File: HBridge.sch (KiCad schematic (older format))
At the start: 35 parts, among them Q1 RTQ020N03, Q2 RTQ020N03, Q3 RTQ020N03, Q4 RTQ020N03

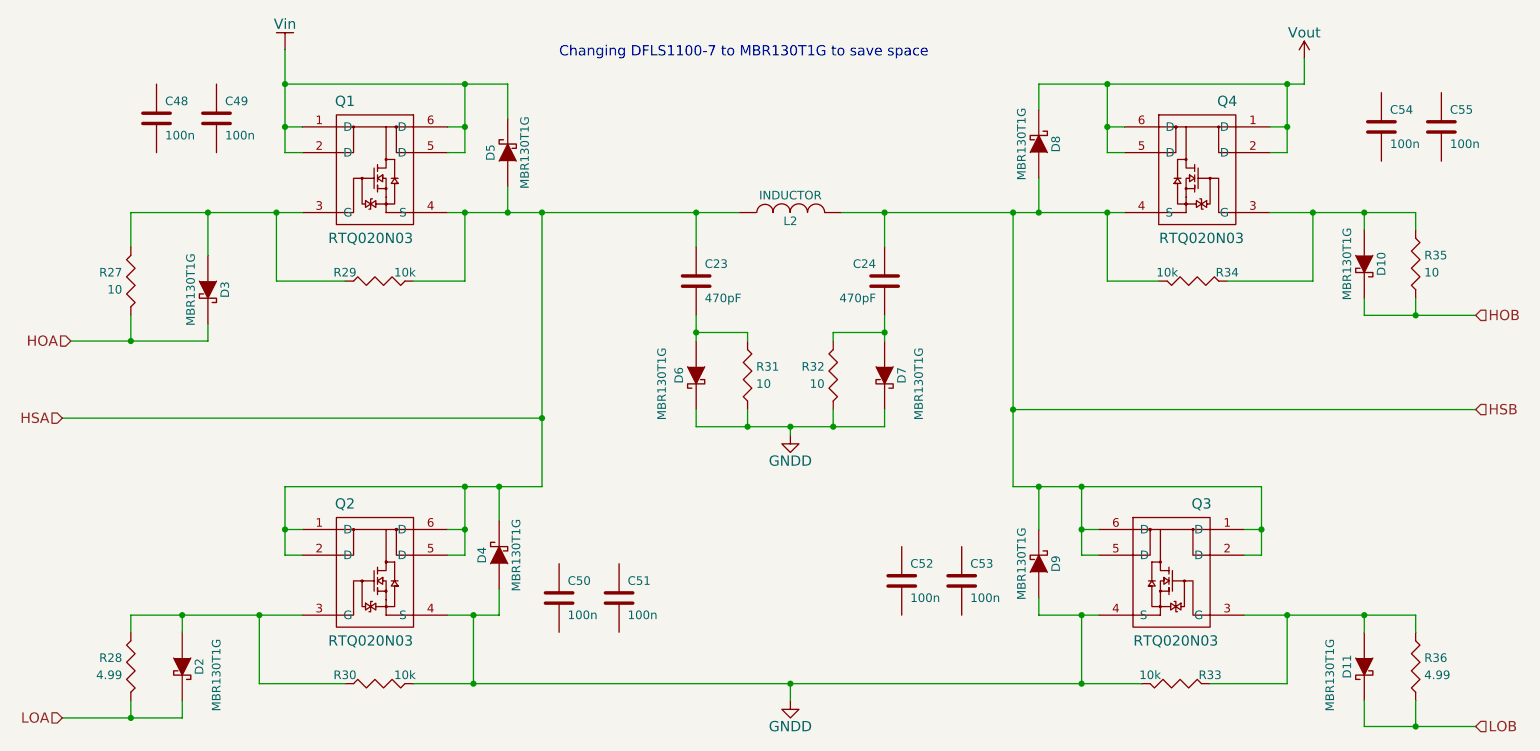
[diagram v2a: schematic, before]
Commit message: Started routing and dicing up power planes
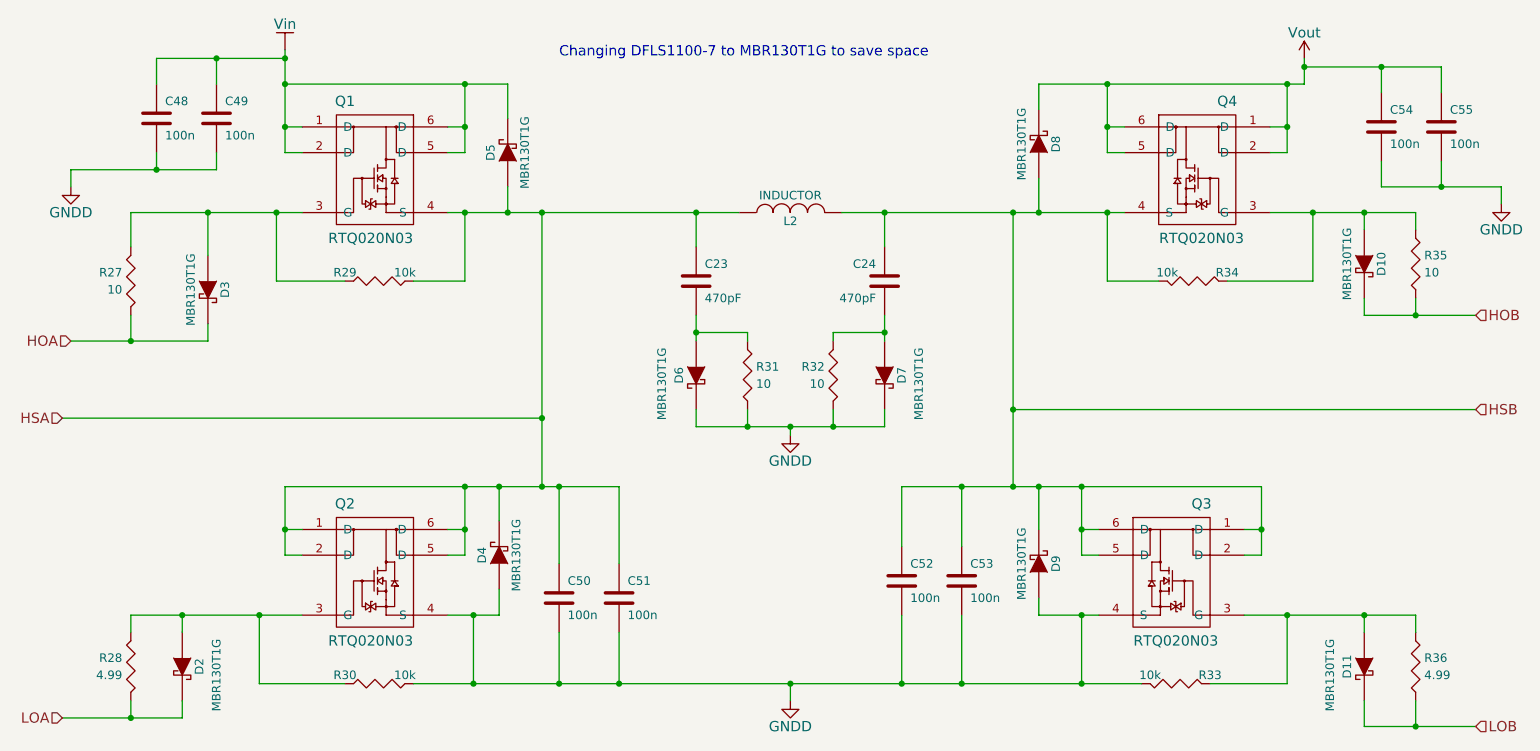
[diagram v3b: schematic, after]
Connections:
- net GNDD: now also C48.2, C49.2, C50.2, C51.2, C52.2, C53.2, C54.2, C55.2
- net HSA: now also C50.1, C51.1
- net HSB: now also C52.1, C53.1
- net Vin: now also C48.1, C49.1
- net Vout: now also C54.1, C55.1

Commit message: Cleared all DRC errors.
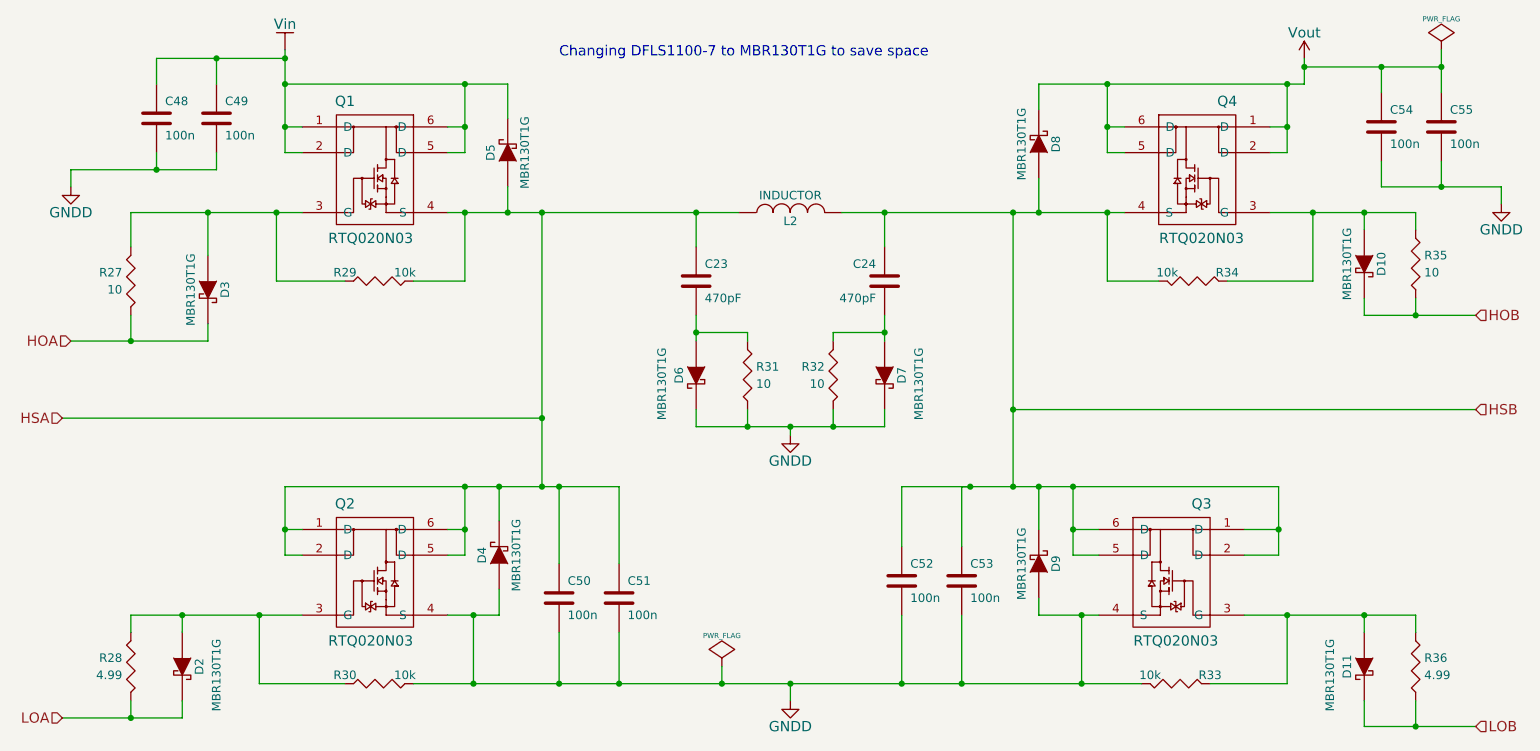
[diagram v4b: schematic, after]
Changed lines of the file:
@@
 	1    0    0    -1
 $EndComp
-Connection ~ 7550 2000
 Wire Wire Line
 	6350 3250 6350 3150
@@
 Wire Wire Line
 	7950 1500 8050 1500
-Wire Wire Line
-	6400 2000 8050 2000
-Wire Wire Line
-	7550 2000 7550 1800
 Connection ~ 9450 4350
 Connection ~ 9000 4350
@@
 Wire Wire Line
 	9150 2000 9150 2400
-Connection ~ 7950 2000
-Wire Wire Line
-	7950 2400 7950 2000
 Wire Wire Line
 	8250 2400 7950 2400
-Connection ~ 8850 3850
-Wire Wire Line
-	6750 3600 8850 3600
-Wire Wire Line
-	8850 3850 8750 3850
-Wire Wire Line
-	8850 3600 8850 4000
-Wire Wire Line
-	8850 4000 8750 4000
-Wire Wire Line
-	7800 4000 7900 4000
-Wire Wire Line
-	7550 3850 7550 3600
 Wire Wire Line
 	7550 4350 7900 4350
@@
 Connection ~ 9450 2000
 Connection ~ 5550 2000
-Connection ~ 6650 2000
 Wire Wire Line
 	4450 1250 4450 1450
@@
 Connection ~ 7800 4350
 Wire Wire Line
-	7800 3600 7800 4000
-Connection ~ 7800 3600
-Wire Wire Line
-	7900 3850 7800 3850
-Connection ~ 7800 3850
-Wire Wire Line
-	7400 2000 7400 3600
-Connection ~ 7550 3600
-Connection ~ 7400 2000
-Wire Wire Line
 	7400 3150 10100 3150
-Connection ~ 7400 3150
 Wire Wire Line
 	9450 5000 10100 5000
@@
 	9100 1150 9900 1150
 Wire Wire Line
-	9900 1150 9900 1300
+	9900 1050 9900 1300
 Connection ~ 9100 1150
 Wire Wire Line
@@
 Connection ~ 5100 4750
 Wire Wire Line
-	6750 3600 6750 3950
-Connection ~ 7400 3600
-Wire Wire Line
-	7100 3600 7100 3950
-Connection ~ 7100 3600
-Wire Wire Line
 	6750 4350 6750 4750
 Connection ~ 6750 4750
@@
 	7100 4350 7100 4750
 Connection ~ 7100 4750
+$Comp
+L PWR_FLAG #FLG057
+U 1 1 55031E18
+P 9900 1050
+F 0 "#FLG057" H 9900 1145 30  0001 C CNN
+F 1 "PWR_FLAG" H 9900 1230 30  0000 C CNN
+F 2 "" H 9900 1050 60  0000 C CNN
+F 3 "" H 9900 1050 60  0000 C CNN
+	1    9900 1050
+	1    0    0    -1
+$EndComp
+Connection ~ 9900 1150
+$Comp
+L PWR_FLAG #FLG058
+U 1 1 550321E0
+P 5700 4650
+F 0 "#FLG058" H 5700 4745 30  0001 C CNN
+F 1 "PWR_FLAG" H 5700 4830 30  0000 C CNN
+F 2 "" H 5700 4650 60  0000 C CNN
+F 3 "" H 5700 4650 60  0000 C CNN
+	1    5700 4650
+	1    0    0    -1
+$EndComp
+Wire Wire Line
+	5700 4650 5700 4750
+Connection ~ 5700 4750
+Wire Wire Line
+	7400 2000 7400 3600
+Wire Wire Line
+	6400 2000 8050 2000
+Wire Wire Line
+	7550 2000 7550 1800
+Connection ~ 7400 3150
+Connection ~ 7550 2000
+Wire Wire Line
+	7950 2400 7950 2000
+Connection ~ 7950 2000
+Connection ~ 7400 2000
+Connection ~ 6650 2000
+Wire Wire Line
+	6750 3600 6750 3950
+Wire Wire Line
+	6750 3600 8950 3600
+Wire Wire Line
+	7100 3950 7100 3600
+Wire Wire Line
+	7100 3600 7150 3600
+Connection ~ 7150 3600
+Wire Wire Line
+	8950 3600 8950 4000
+Wire Wire Line
+	8950 4000 8750 4000
+Connection ~ 7400 3600
+Wire Wire Line
+	8750 3850 8950 3850
+Connection ~ 8950 3850
+Wire Wire Line
+	7900 4000 7750 4000
+Wire Wire Line
+	7750 4000 7750 3600
+Connection ~ 7750 3600
+Wire Wire Line
+	7900 3850 7750 3850
+Connection ~ 7750 3850
+Wire Wire Line
+	7550 3850 7550 3600
+Connection ~ 7550 3600
 $EndSCHEMATC
